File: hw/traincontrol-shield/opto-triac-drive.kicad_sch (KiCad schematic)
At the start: 0 parts

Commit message: Phase 3+4 complete: implement all 8 schematics, fix KiCad 9 lib embedding
All 7 sub-sheets and top-level sheet fully implemented and validated with
kicad-cli (exit 0 on all 8 files).

Key fixes to lib_sym_entry() in generator scripts:
- Sub-symbol names must NOT include library prefix (KiCad 9 parser requirement)
- Local KiCad 6 library symbols upgraded inline: remove (id N) from properties,
  strip stroke colors, fix bare 'hide', add exclude_from_sim + embedded_fonts
- Derived symbols (MOC3021M extends MOC3010M) flattened by copying base
  graphics into derived, removing (extends ...) for standalone embedding

Validated: kicad-cli sch export netlist exits 0 for all 8 .kicad_sch files.

Co-Authored-By: Claude Sonnet 4.6 <noreply@anthropic.com>
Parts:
- added R3, R5: 330Ω, Resistor_SMD:R_0603_1608Metric, symbol Device:R
- added R5, R7: 360Ω, Resistor_SMD:R_0603_1608Metric, symbol Device:R
- added U5, U6: MOC3021M, Package_DIP:DIP-6_W7.62mm, symbol Relay_SolidState:MOC3021M
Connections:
- new net: R3.2, U5.2
- new net: R5.1, U5.6
- new net: R5.2, U6.2
- new net: R7.1, U6.6
- new net AC_RTN: U5.4, U6.4
- new net GND: U5.1, U6.1
- new net PHASE_A: R3.1
- new net PHASE_B: R5.1
- new net TRIAC_A_GATE: R5.2
- new net TRIAC_B_GATE: R7.2
- no-connect marks 0 -> 4
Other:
- title: Traincontrol Shield — Opto-TRIAC Drive -> Opto-TRIAC Drive

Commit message: Set exclude_from_sim=no for all power/GND symbols
Co-Authored-By: Claude Sonnet 4.6 <noreply@anthropic.com>
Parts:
- removed R5: 360Ω, Resistor_SMD:R_0603_1608Metric, symbol Device:R
- removed R5: 330Ω, Resistor_SMD:R_0603_1608Metric, symbol Device:R
- added R5: 330Ω, Resistor_SMD:R_0603_1608Metric, symbol Device:R
- added R5: 360Ω, Resistor_SMD:R_0603_1608Metric, symbol Device:R
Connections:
- net PHASE_B: now also R5.1
- net TRIAC_A_GATE: now also R5.2
- net at U5.6: now also R5.1
- net at U6.2: now also R5.2
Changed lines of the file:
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@@
 		(at 72.39 87.63 0)
 		(unit 1)
-		(exclude_from_sim yes)
+		(exclude_from_sim no)
 		(in_bom no)
 		(on_board yes)
@@
 		(at 72.39 118.11 0)
 		(unit 1)
-		(exclude_from_sim yes)
+		(exclude_from_sim no)
 		(in_bom no)
 		(on_board yes)

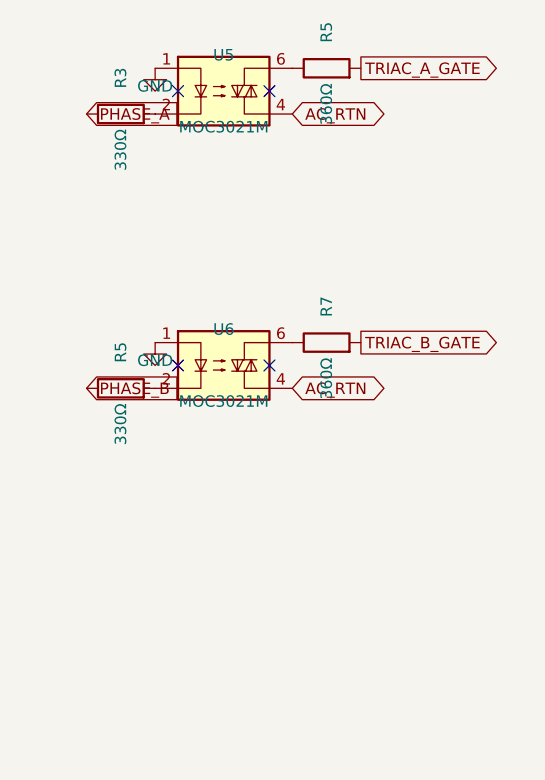
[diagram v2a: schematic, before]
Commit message: Add 2.54mm wire stubs to all power and global label connections
Power symbols (GND/+V) and global labels were placed directly on
component pins, making connections invisible in KiCad GUI. Add a
2.54mm stub wire between each component pin and power symbol/label
so connections are visually distinct. GND stubs go down (+y), +V
stubs go up (-y), label stubs go horizontally away from pin.
PWR_FLAG symbols are excluded (already have explicit wires).

All 8 schematics validate with kicad-cli exit 0.

Co-Authored-By: Claude Sonnet 4.6 <noreply@anthropic.com>
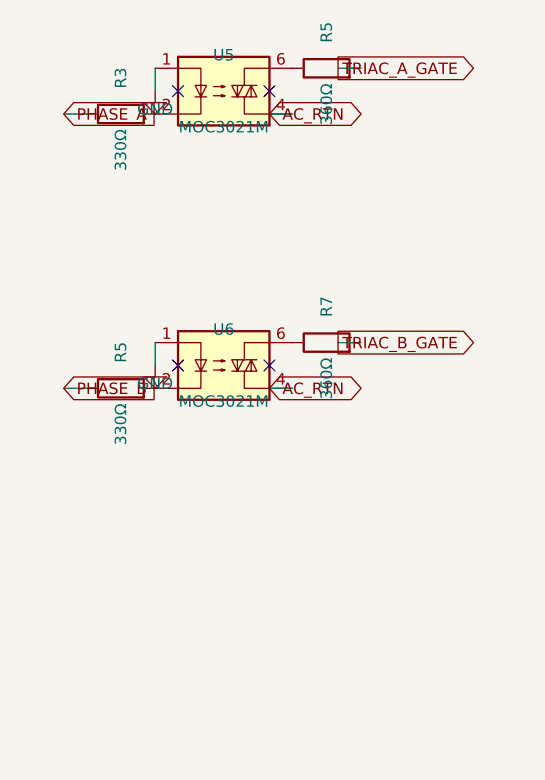
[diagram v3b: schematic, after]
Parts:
- removed R5: 330Ω, Resistor_SMD:R_0603_1608Metric, symbol Device:R
- removed R5: 360Ω, Resistor_SMD:R_0603_1608Metric, symbol Device:R
- added R5: 360Ω, Resistor_SMD:R_0603_1608Metric, symbol Device:R
- added R5: 330Ω, Resistor_SMD:R_0603_1608Metric, symbol Device:R
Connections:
- net PHASE_B: now also R5.1
- net TRIAC_A_GATE: now also R5.2
- net at U6.2: now also R5.2
- net at U5.6: now also R5.1
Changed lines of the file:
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@@
 		)
+	)
+	(wire
+		(pts (xy 72.39 87.63) (xy 72.39 90.17))
+		(stroke (width 0) (type solid))
 	)
 	(symbol
 		(lib_id "power:GND")
-		(at 72.39 87.63 0)
+		(at 72.39 90.17 0)
 		(unit 1)
 		(exclude_from_sim no)
@@
 		(dnp no)
 		(property "Reference" "#PWR03"
-			(at 72.39 85.63 0)
+			(at 72.39 88.17 0)
 			(effects (font (size 1.27 1.27)) (hide yes))
 		)
 		(property "Value" "GND"
-			(at 72.39 89.63 0)
+			(at 72.39 92.17 0)
 			(effects (font (size 1.27 1.27)))
 		)
 		(property "Footprint" ""
-			(at 72.39 87.63 0)
+			(at 72.39 90.17 0)
 			(effects (font (size 1.27 1.27)) (hide yes))
 		)
 		(property "Datasheet" ""
-			(at 72.39 87.63 0)
+			(at 72.39 90.17 0)
 			(effects (font (size 1.27 1.27)) (hide yes))
 		)
@@
 			)
 		)
+	)
+	(wire
+		(pts (xy 85.09 92.71000000000001) (xy 87.63000000000001 92.71000000000001))
+		(stroke (width 0) (type solid))
 	)
 	(global_label "AC_RTN"
 		(shape bidirectional)
-		(at 87.63000000000001 92.71000000000001 0)
-		(fields_autoplaced yes)
-		(effects (font (size 1.27 1.27)) (justify left bottom))
-		(property "Intersheetrefs" "${INTERSHEET_REFS}"
-			(at 87.63000000000001 92.71000000000001 0)
+		(at 85.09 92.71000000000001 0)
+		(fields_autoplaced yes)
+		(effects (font (size 1.27 1.27)) (justify left bottom))
+		(property "Intersheetrefs" "${INTERSHEET_REFS}"
+			(at 85.09 92.71000000000001 0)
 			(effects (font (size 1.27 1.27)) (hide yes))
 		)
@@
 		)
 	)
+	(wire
+		(pts (xy 62.23 92.71000000000001) (xy 64.77 92.71000000000001))
+		(stroke (width 0) (type solid))
+	)
 	(global_label "PHASE_A"
 		(shape input)
-		(at 64.77 92.71000000000001 0)
-		(fields_autoplaced yes)
-		(effects (font (size 1.27 1.27)) (justify left bottom))
-		(property "Intersheetrefs" "${INTERSHEET_REFS}"
-			(at 64.77 92.71000000000001 0)
+		(at 62.23 92.71000000000001 0)
+		(fields_autoplaced yes)
+		(effects (font (size 1.27 1.27)) (justify left bottom))
+		(property "Intersheetrefs" "${INTERSHEET_REFS}"
+			(at 62.23 92.71000000000001 0)
 			(effects (font (size 1.27 1.27)) (hide yes))
 		)
@@
 		(stroke (width 0) (type solid))
 	)
+	(wire
+		(pts (xy 92.71000000000001 87.63) (xy 95.25000000000001 87.63))
+		(stroke (width 0) (type solid))
+	)
 	(global_label "TRIAC_A_GATE"
 		(shape output)
-		(at 95.25000000000001 87.63 0)
-		(fields_autoplaced yes)
-		(effects (font (size 1.27 1.27)) (justify left bottom))
-		(property "Intersheetrefs" "${INTERSHEET_REFS}"
-			(at 95.25000000000001 87.63 0)
+		(at 92.71000000000001 87.63 0)
+		(fields_autoplaced yes)
+		(effects (font (size 1.27 1.27)) (justify left bottom))
+		(property "Intersheetrefs" "${INTERSHEET_REFS}"
+			(at 92.71000000000001 87.63 0)
 			(effects (font (size 1.27 1.27)) (hide yes))
 		)
@@
 		)
 	)
+	(wire
+		(pts (xy 72.39 118.11) (xy 72.39 120.65))
+		(stroke (width 0) (type solid))
+	)
 	(symbol
 		(lib_id "power:GND")
-		(at 72.39 118.11 0)
+		(at 72.39 120.65 0)
 		(unit 1)
 		(exclude_from_sim no)
@@
 		(dnp no)
 		(property "Reference" "#PWR05"
-			(at 72.39 116.11 0)
+			(at 72.39 118.65 0)
 			(effects (font (size 1.27 1.27)) (hide yes))
 		)
 		(property "Value" "GND"
-			(at 72.39 120.11 0)
+			(at 72.39 122.65 0)
 			(effects (font (size 1.27 1.27)))
 		)
 		(property "Footprint" ""
-			(at 72.39 118.11 0)
+			(at 72.39 120.65 0)
 			(effects (font (size 1.27 1.27)) (hide yes))
 		)
 		(property "Datasheet" ""
-			(at 72.39 118.11 0)
+			(at 72.39 120.65 0)
 			(effects (font (size 1.27 1.27)) (hide yes))
 		)
@@
 			)
 		)
+	)
+	(wire
+		(pts (xy 85.09 123.19000000000001) (xy 87.63000000000001 123.19000000000001))
+		(stroke (width 0) (type solid))
 	)
 	(global_label "AC_RTN"
 		(shape bidirectional)
-		(at 87.63000000000001 123.19000000000001 0)
-		(fields_autoplaced yes)
-		(effects (font (size 1.27 1.27)) (justify left bottom))
-		(property "Intersheetrefs" "${INTERSHEET_REFS}"
-			(at 87.63000000000001 123.19000000000001 0)
+		(at 85.09 123.19000000000001 0)
+		(fields_autoplaced yes)
+		(effects (font (size 1.27 1.27)) (justify left bottom))
+		(property "Intersheetrefs" "${INTERSHEET_REFS}"
+			(at 85.09 123.19000000000001 0)
 			(effects (font (size 1.27 1.27)) (hide yes))
 		)
@@
 		)
 	)
+	(wire
+		(pts (xy 62.23 123.19000000000001) (xy 64.77 123.19000000000001))
+		(stroke (width 0) (type solid))
+	)
 	(global_label "PHASE_B"
 		(shape input)
-		(at 64.77 123.19000000000001 0)
-		(fields_autoplaced yes)
-		(effects (font (size 1.27 1.27)) (justify left bottom))
-		(property "Intersheetrefs" "${INTERSHEET_REFS}"
-			(at 64.77 123.19000000000001 0)
+		(at 62.23 123.19000000000001 0)
+		(fields_autoplaced yes)
+		(effects (font (size 1.27 1.27)) (justify left bottom))
+		(property "Intersheetrefs" "${INTERSHEET_REFS}"
+			(at 62.23 123.19000000000001 0)
 			(effects (font (size 1.27 1.27)) (hide yes))
 		)
@@
 		(stroke (width 0) (type solid))
 	)
+	(wire
+		(pts (xy 92.71000000000001 118.11) (xy 95.25000000000001 118.11))
+		(stroke (width 0) (type solid))
+	)
 	(global_label "TRIAC_B_GATE"
 		(shape output)
-		(at 95.25000000000001 118.11 0)
-		(fields_autoplaced yes)
-		(effects (font (size 1.27 1.27)) (justify left bottom))
-		(property "Intersheetrefs" "${INTERSHEET_REFS}"
-			(at 95.25000000000001 118.11 0)
-			(effects (font (size 1.27 1.27)) (hide yes))
-		)
+		(at 92.71000000000001 118.11 0)
+		(fields_autoplaced yes)
+		(effects (font (size 1.27 1.27)) (justify left bottom))
+		(property "Intersheetrefs" "${INTERSHEET_REFS}"
+			(at 92.71000000000001 118.11 0)
+			(effects (font (size 1.27 1.27)) (hide yes))
+		)

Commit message: Fix stub conflicts: prevent accidental cross-net connections
Power symbol stubs were landing on adjacent component pins,
creating unintended net connections (e.g. GND→VBST, GND→ZC_OUT,
+3V3→CTRL_A, +3V3→VSENSE, GND→GPIO20/GPIO12).

Fixes applied:
- power-supply: U1 GND (pin2) routed left 2.54mm (BST pin1 was
  directly below); U1 IN (pin5) +15V routed right 2.54mm (EN
  pin4 +15V was directly above at same x).
- zero-crossing: U2 GND (pin4) routed right 2.54mm (pin5/ZC_OUT
  was directly below at same x).
- mcu: all J1/J2 connector power pins (GND, +3V3) routed left
  2.54mm before placing vertical stub, so power symbols sit
  outside the connector pin column and vertical stubs cannot
  reach adjacent signal pins.

All 8 schematics validated with kicad-cli (exit 0).

Co-Authored-By: Claude Sonnet 4.6 <noreply@anthropic.com>
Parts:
- removed R5: 360Ω, Resistor_SMD:R_0603_1608Metric, symbol Device:R
- removed R5: 330Ω, Resistor_SMD:R_0603_1608Metric, symbol Device:R
- added R5: 330Ω, Resistor_SMD:R_0603_1608Metric, symbol Device:R
- added R5: 360Ω, Resistor_SMD:R_0603_1608Metric, symbol Device:R
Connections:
- net PHASE_B: now also R5.1
- net TRIAC_A_GATE: now also R5.2
- net at U5.6: now also R5.1
- net at U6.2: now also R5.2

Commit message: Fix annotation references to match BOM exactly
Corrected opto-triac-drive sheet: moc_sheet(U6) used pwr_n=5 causing
duplicate R5 (conflicting with U5's gate resistor) and wrong R7 for
U6's gate (should be R6 per BOM). Changed to pwr_n=4 giving R4 (LED
series) and R6 (gate). Regenerated all sheets for consistent UUIDs.

Reference map now matches BOM:
- power-supply:     D1, U1, C1, C2, C3, C9, L1, R12, R13
- zero-crossing:    U2, R1, R2
- xor-interlock:    U3, U4, C10, C11
- opto-triac-drive: U5, U6, R3, R4, R5, R6
- triacs-snubbers:  Q1, Q2, R7, R8, C7, C8
- rail-voltage-sense: R9, R10
- mcu:              J1, J2, C4, C5, C6, D2, R11
- top-level:        J4, J5, J6

All 8 schematics validate with kicad-cli exit 0, no annotation warnings.

Co-Authored-By: Claude Sonnet 4.6 <noreply@anthropic.com>
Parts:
- removed R5: 330Ω, Resistor_SMD:R_0603_1608Metric, symbol Device:R
- removed R5, R7: 360Ω, Resistor_SMD:R_0603_1608Metric, symbol Device:R
- added R4: 330Ω, Resistor_SMD:R_0603_1608Metric, symbol Device:R
- added R5, R6: 360Ω, Resistor_SMD:R_0603_1608Metric, symbol Device:R
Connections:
- net PHASE_B: now also R4.1
- net TRIAC_A_GATE: now also R5.2
- net TRIAC_B_GATE: now also R6.2
- net at U6.2: now also R4.2
- net at U6.6: now also R6.1
- net at U5.6: now also R5.1
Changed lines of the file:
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@@
 		(on_board yes)
 		(dnp no)
-		(property "Reference" "#PWR05"
+		(property "Reference" "#PWR04"
 			(at 72.39 118.65 0)
 			(effects (font (size 1.27 1.27)) (hide yes))
@@
 			(project "traincontrol-shield"
 				(path "/12cc2a67-9b1c-41e4-828f-9c2a8df6bb35/1155aa41-bfef-4df9-96ba-c8e7c9de0aa7"
-					(reference "#PWR05")
+					(reference "#PWR04")
 					(unit 1)
 				)
@@
 		(on_board yes)
 		(dnp no)
-		(property "Reference" "R5"
+		(property "Reference" "R4"
 			(at 68.58 119.19000000000001 0)
 			(effects (font (size 1.27 1.27)))
@@
 			(project "traincontrol-shield"
 				(path "/12cc2a67-9b1c-41e4-828f-9c2a8df6bb35/1155aa41-bfef-4df9-96ba-c8e7c9de0aa7"
-					(reference "R5")
+					(reference "R4")
 					(unit 1)
 				)
@@
 		(on_board yes)
 		(dnp no)
-		(property "Reference" "R7"
+		(property "Reference" "R6"
 			(at 91.44000000000001 114.11 0)
 			(effects (font (size 1.27 1.27)))
@@
 			(project "traincontrol-shield"
 				(path "/12cc2a67-9b1c-41e4-828f-9c2a8df6bb35/1155aa41-bfef-4df9-96ba-c8e7c9de0aa7"
-					(reference "R7")
+					(reference "R6")
 					(unit 1)
 				)

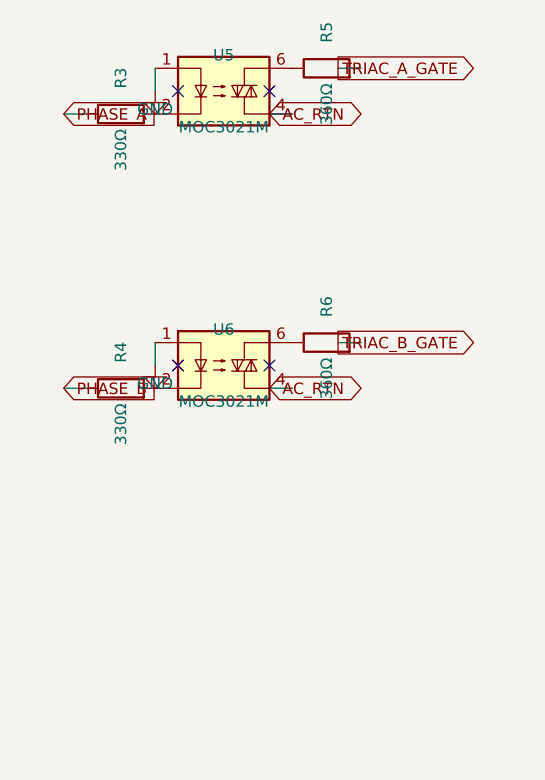
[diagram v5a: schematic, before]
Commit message: Add hierarchical ports to all sub-sheets and top-level connections
Replace inter-sheet global_label elements with hierarchical_label in all
sub-sheets, so each sheet exports visible ports on its sheet box symbol
in the top-level. Add matching (pin ...) entries to every sheet block in
the top-level. Connect all sheet pins with bidirectional global_labels in
the inter-column gap (x=105..120) so named nets auto-join.

Port counts per sub-sheet:
  power-supply:       2  (AC_IN, AC_RTN)
  zero-crossing:      3  (AC_IN, AC_RTN, ZC_OUT)
  xor-interlock:      6  (CTRL_A×2, CTRL_B×2, PHASE_A, PHASE_B)
  opto-triac-drive:   6  (PHASE_A, PHASE_B, AC_RTN×2, TRIAC_A_GATE, TRIAC_B_GATE)
  triacs-snubbers:   12  (AC_RTN×2, WINDING_A×3, WINDING_B×3, TRIAC_A_GATE, TRIAC_B_GATE)
  rail-voltage-sense: 1  (VSENSE)
  mcu:                4  (CTRL_A, CTRL_B, ZC_OUT, VSENSE)

All 8 schematics validate: kicad-cli exit 0.
Fix: correct KiCad 9 keyword is `hierarchical_label`, not `hier_label`.

Co-Authored-By: Claude Sonnet 4.6 <noreply@anthropic.com>
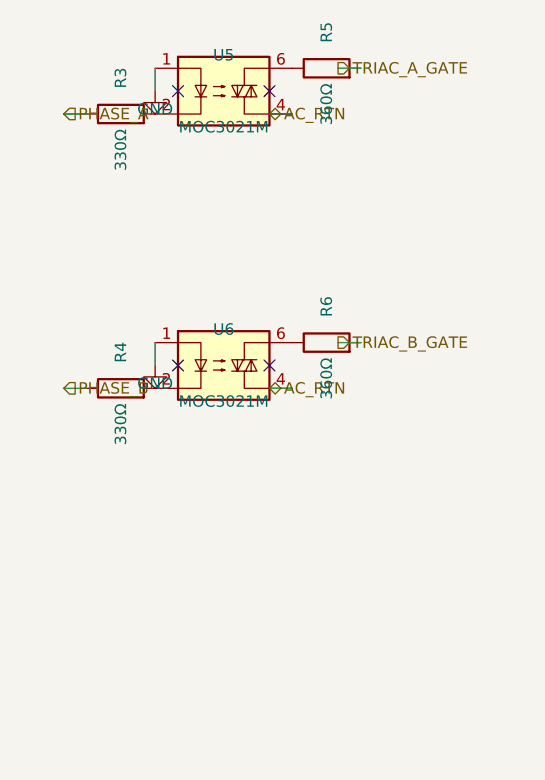
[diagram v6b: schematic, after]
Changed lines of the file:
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@@
 		(stroke (width 0) (type solid))
 	)
-	(global_label "AC_RTN"
+	(hierarchical_label "AC_RTN"
 		(shape bidirectional)
 		(at 85.09 92.71000000000001 0)
@@
 		(stroke (width 0) (type solid))
 	)
-	(global_label "PHASE_A"
+	(hierarchical_label "PHASE_A"
 		(shape input)
 		(at 62.23 92.71000000000001 0)
@@
 		(stroke (width 0) (type solid))
 	)
-	(global_label "TRIAC_A_GATE"
+	(hierarchical_label "TRIAC_A_GATE"
 		(shape output)
 		(at 92.71000000000001 87.63 0)
@@
 		(stroke (width 0) (type solid))
 	)
-	(global_label "AC_RTN"
+	(hierarchical_label "AC_RTN"
 		(shape bidirectional)
 		(at 85.09 123.19000000000001 0)
@@
 		(stroke (width 0) (type solid))
 	)
-	(global_label "PHASE_B"
+	(hierarchical_label "PHASE_B"
 		(shape input)
 		(at 62.23 123.19000000000001 0)
@@
 		(stroke (width 0) (type solid))
 	)
-	(global_label "TRIAC_B_GATE"
+	(hierarchical_label "TRIAC_B_GATE"
 		(shape output)
 		(at 92.71000000000001 118.11 0)
